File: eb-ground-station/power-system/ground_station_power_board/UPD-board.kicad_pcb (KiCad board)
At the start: 2 copper layers, 140.7 x 86.5 mm, 185 parts, among them J1 Conn_01x04, J10 PI 1827486, J11 PC 1720806, J12 Conn_02x02_Odd_Even, J13 Conn_01x05, J14 Conn_01x04, J2 Conn_01x03, J3 Conn_01x03, J4 Conn_01x03, J5 Conn_01x03, J6 Conn_01x03, J7 PI 1924143, J8 PI 1827923, J9 PI 1827486, Q1 DMN61D8L-LVT, Q10 DMN61D8L-LVT, Q11 SUD50P08-25L-E3, Q12 SUD50P08-25L-E3, Q13 DMN61D8L-LVT, Q14 DMN61D8L-LVT, Q15 DMN61D8L-LVT, Q16 DMN61D8L-LVT, Q17 DMN61D8L-LVT, Q18 DMN61D8L-LVT, Q19 DMN61D8L-LVT, Q2 SUD50P08-25L-E3, Q20 DMN61D8L-LVT, Q21 SUD50P08-25L-E3, Q22 SUD50P08-25L-E3, Q3 SUD50P08-25L-E3, Q4 DMN61D8L-LVT, Q5 SUD50P08-25L-E3, Q6 SUD50P08-25L-E3, Q7 DMN61D8L-LVT, Q8 SUD50P08-25L-E3, Q9 SUD50P08-25L-E3, U1 MAX7310, U10 TC4427, U11 TC4427, U12 TC4427, U13 TC4427, U14 TC4427, U15 TC4427, U2 MAX7310, U3 MAX7310, U4 ADT7410TRZ, U5 ADS1115IDGS, U6 UA78M33, U7 U_RasPi_40pin, U8 TC4427, U9 TC4427

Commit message: rev2.1 should be done
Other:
- board text added: "Designed by Benjamin Crall, Miles Simpson, Oliver Rew, and KJ7SU for PSAS"
- board text added: "GitHub Docs"
- board text removed: "Designed by Benjamin Crall"

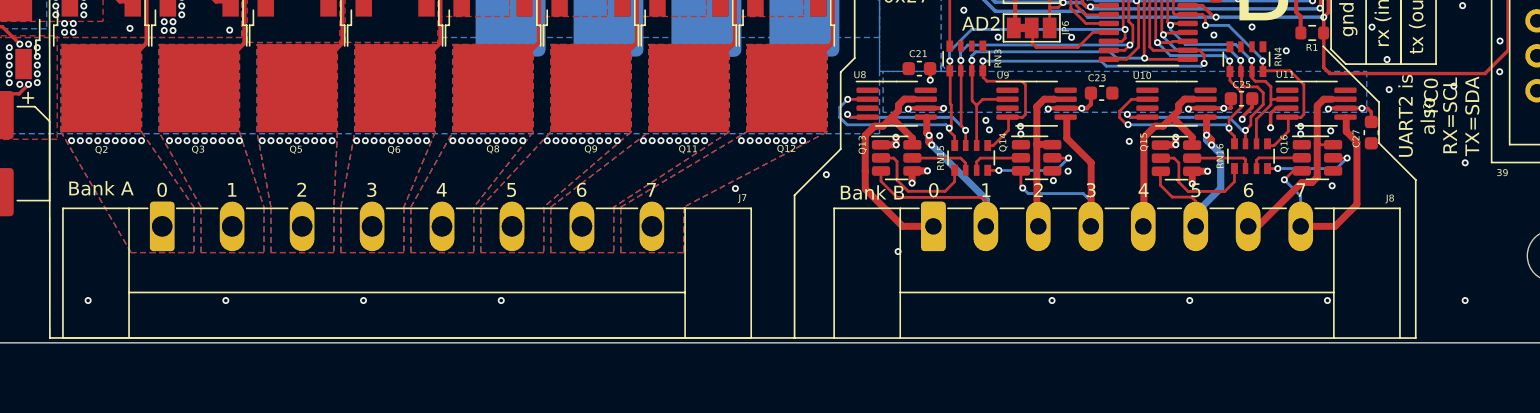
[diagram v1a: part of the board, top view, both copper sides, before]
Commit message: Moved vias out from under test
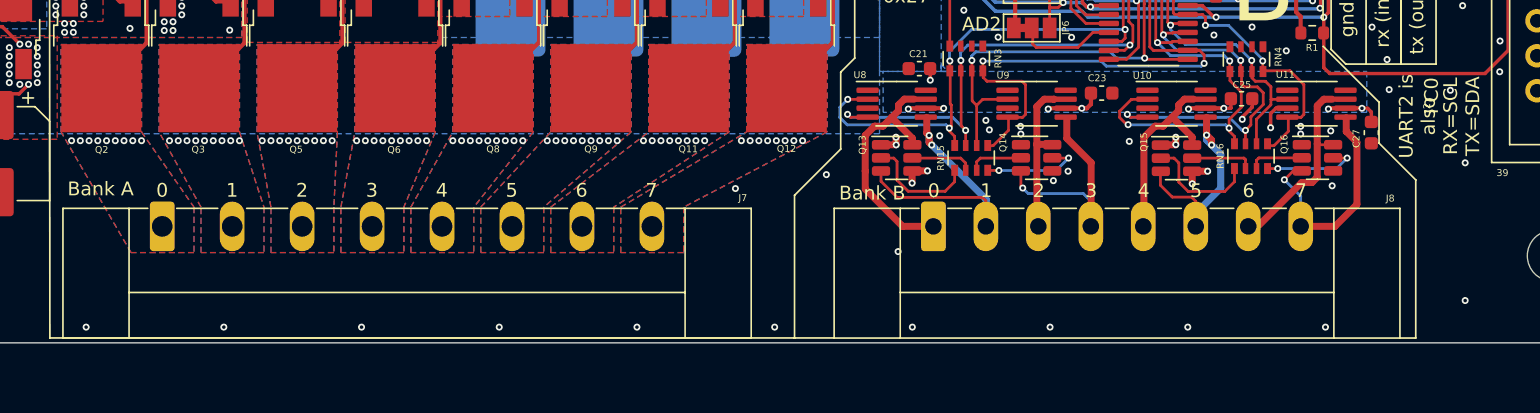
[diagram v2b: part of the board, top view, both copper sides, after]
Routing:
- net GND: vias 274 -> 277
